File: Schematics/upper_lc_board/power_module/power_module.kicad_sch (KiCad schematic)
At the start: 28 parts, among them U13 ID_LM66100DCKR, U14 ID_LM66100DCKR

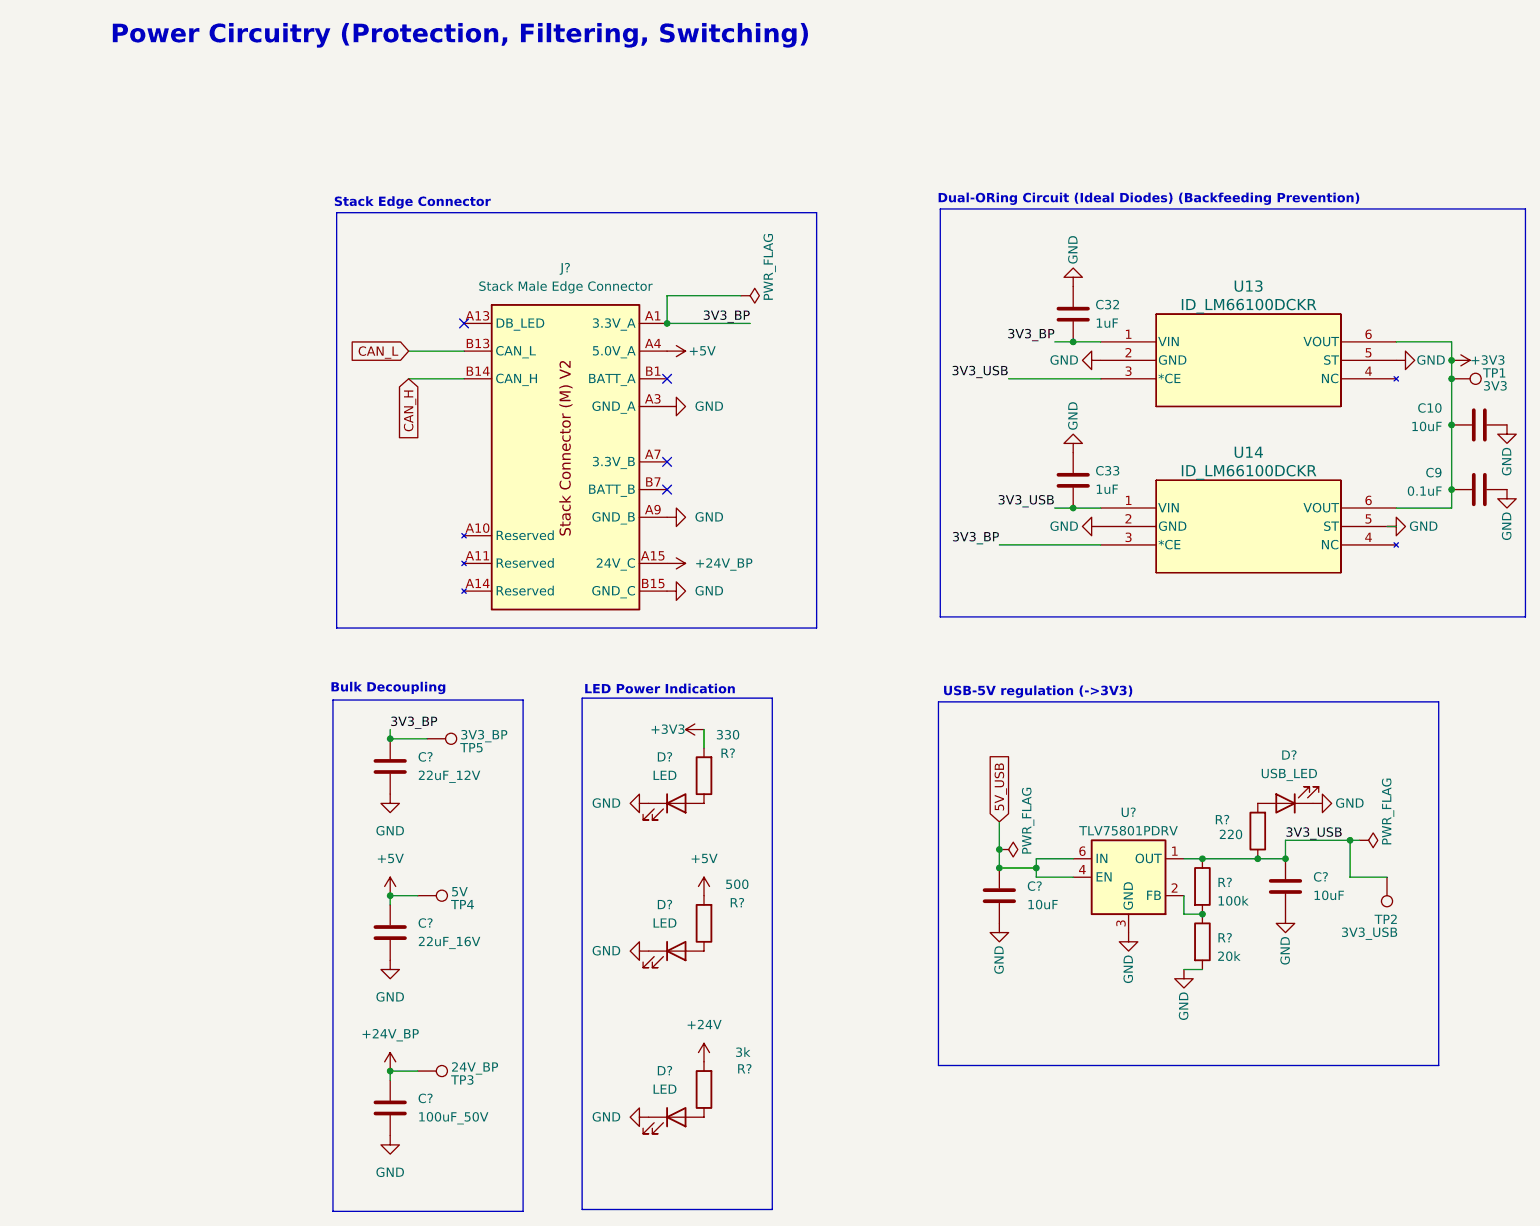
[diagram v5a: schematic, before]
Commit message: Updated all gpio for better routing, > - removed diode array, and 5v sensing > - added dedicated clk generator for adc
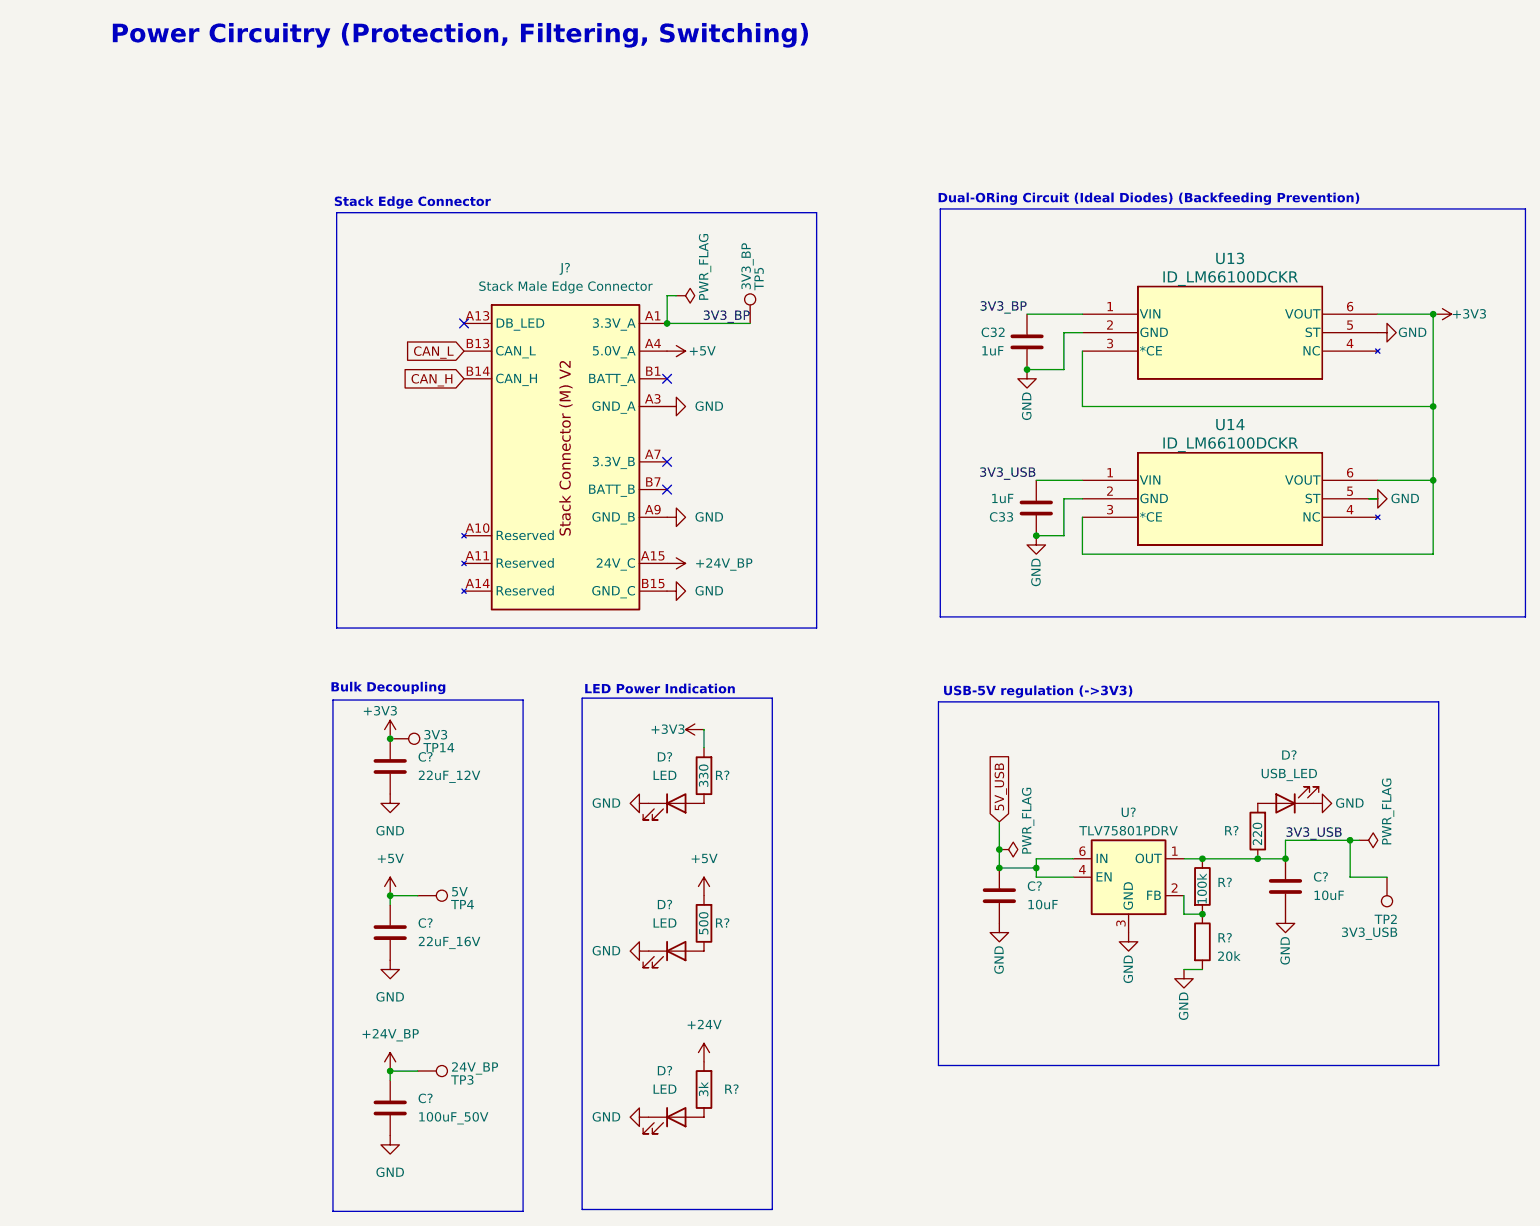
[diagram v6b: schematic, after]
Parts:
- removed C10: 10uF, Capacitor_SMD:C_0603_1608Metric, symbol Device:C
- removed C9: 0.1uF, Capacitor_SMD:C_0603_1608Metric, symbol Device:C
- removed TP1: 3V3, TestPoint:TestPoint_Pad_D1.0mm, symbol Connector:TestPoint
- added TP14: 3V3, TestPoint:TestPoint_Pad_D1.0mm, symbol Connector:TestPoint
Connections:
- net +3V3: now also C?.1, U13.3 (*CE), U14.3 (*CE), TP14.1
- net 3V3_BP: now also C32.2; no longer C32.1, C?.1, U14.3 (*CE)
- net 3V3_USB: no longer U13.3 (*CE)
- net GND: now also C32.1; no longer C32.2
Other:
- moved on the sheet: C32, C33, TP5, U13, U14

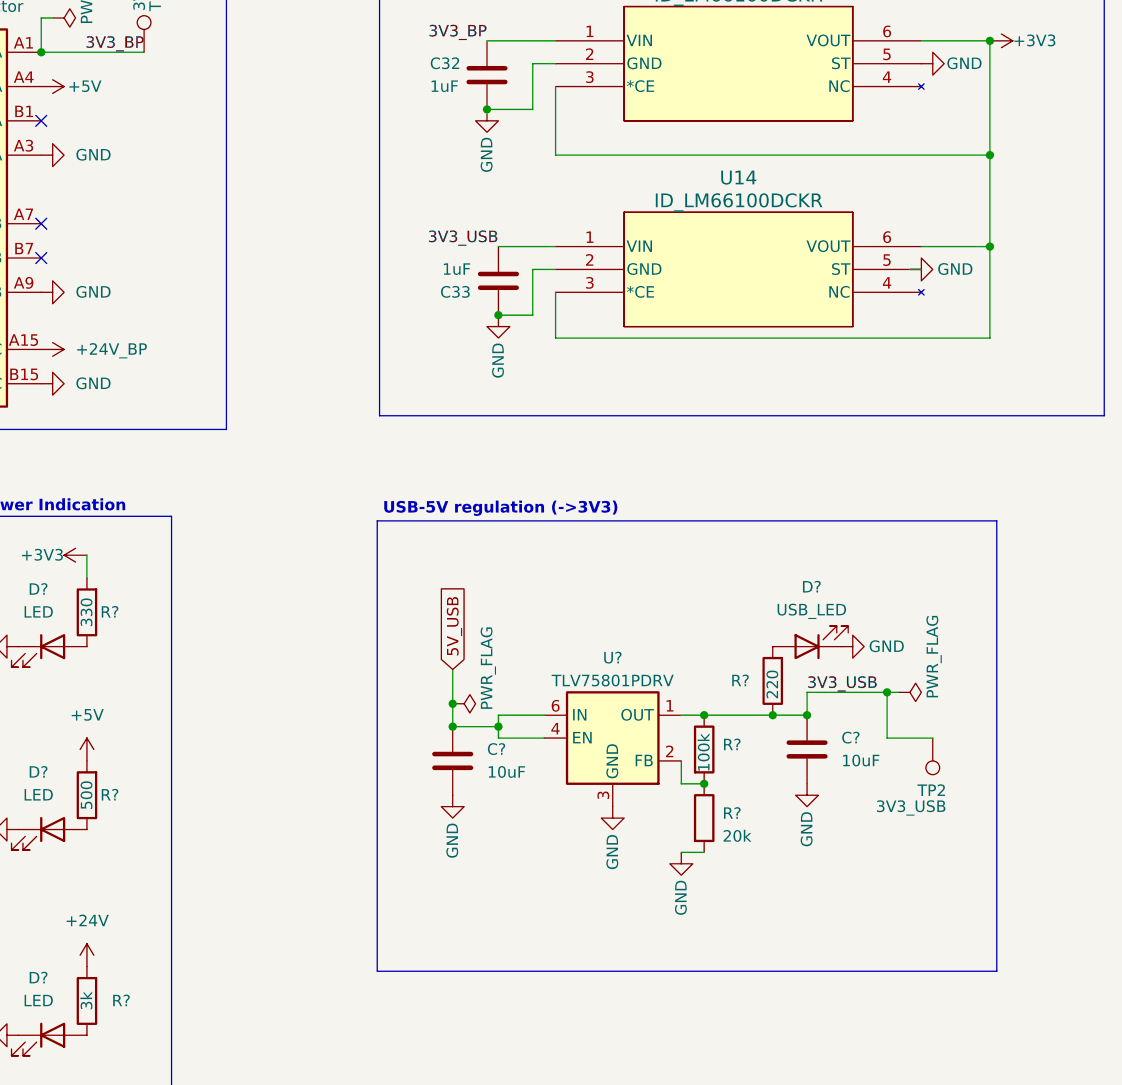
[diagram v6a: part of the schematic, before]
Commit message: added serial comm support and automatic flashing via uart bridge
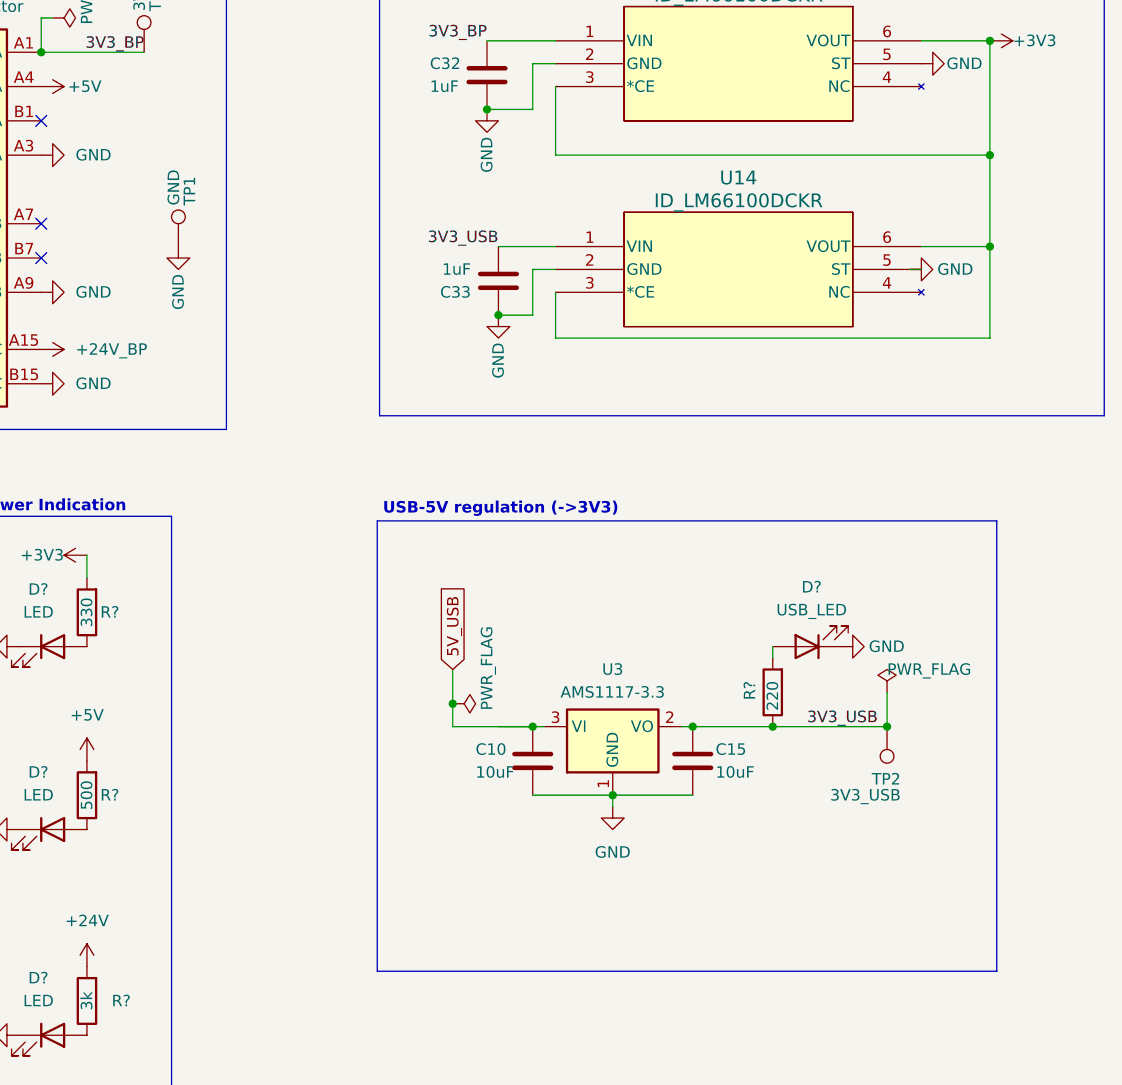
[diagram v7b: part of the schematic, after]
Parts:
- removed C? (x2): 10uF, Capacitor_SMD:C_0603_1608Metric, symbol Device:C
- removed R?: 20k, Resistor_SMD:R_0402_1005Metric, symbol Device:R
- removed R?: 100k, Resistor_SMD:R_0402_1005Metric, symbol Device:R
- removed U?: TLV75801PDRV, Package_SON:WSON-6-1EP_2x2mm_P0.65mm_EP1x1.6mm, symbol Regulator_Linear:TLV75801PDRV
- added C10, C15: 10uF, Capacitor_SMD:C_0603_1608Metric, symbol Device:C
- added TP1: GND, TestPoint:TestPoint_Pad_D1.0mm, symbol Connector:TestPoint
- added U3: AMS1117-3.3, Package_TO_SOT_SMD:SOT-223-3_TabPin2, symbol Regulator_Linear:AMS1117-3.3
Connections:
- net 3V3_USB: now also C15.1, U3.2 (VO)
- net 5V_USB: now also C10.1, U3.3 (VI)
- net GND: now also C10.2, C15.2, TP1.1, U3.1 (GND)
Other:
- moved on the sheet: R?, TP2
